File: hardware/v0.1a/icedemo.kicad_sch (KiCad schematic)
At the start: 9 parts

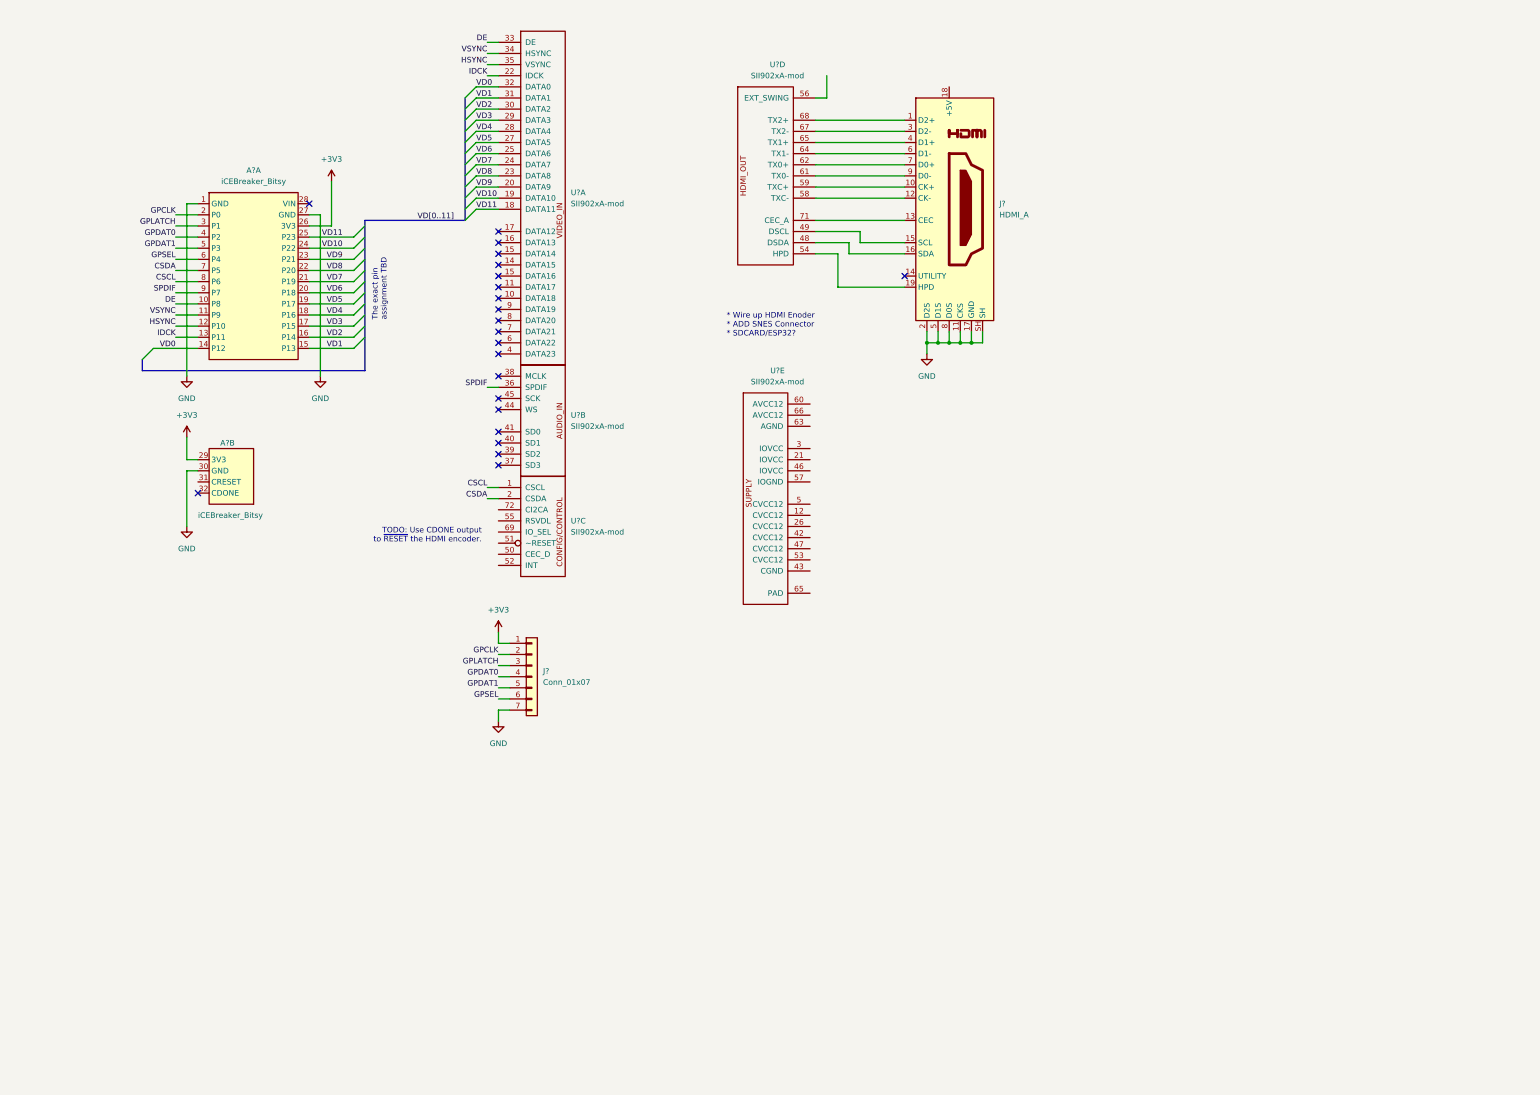
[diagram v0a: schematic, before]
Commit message: First draft of the schematic.
Connected all the remaining pins of the encoder chip.
Replaced the SNES connector generic symbol with a dedicated one.
Added ESD protection to the HDMI connector. (might delete later ;) )
Added level shifters for the SNES interface.
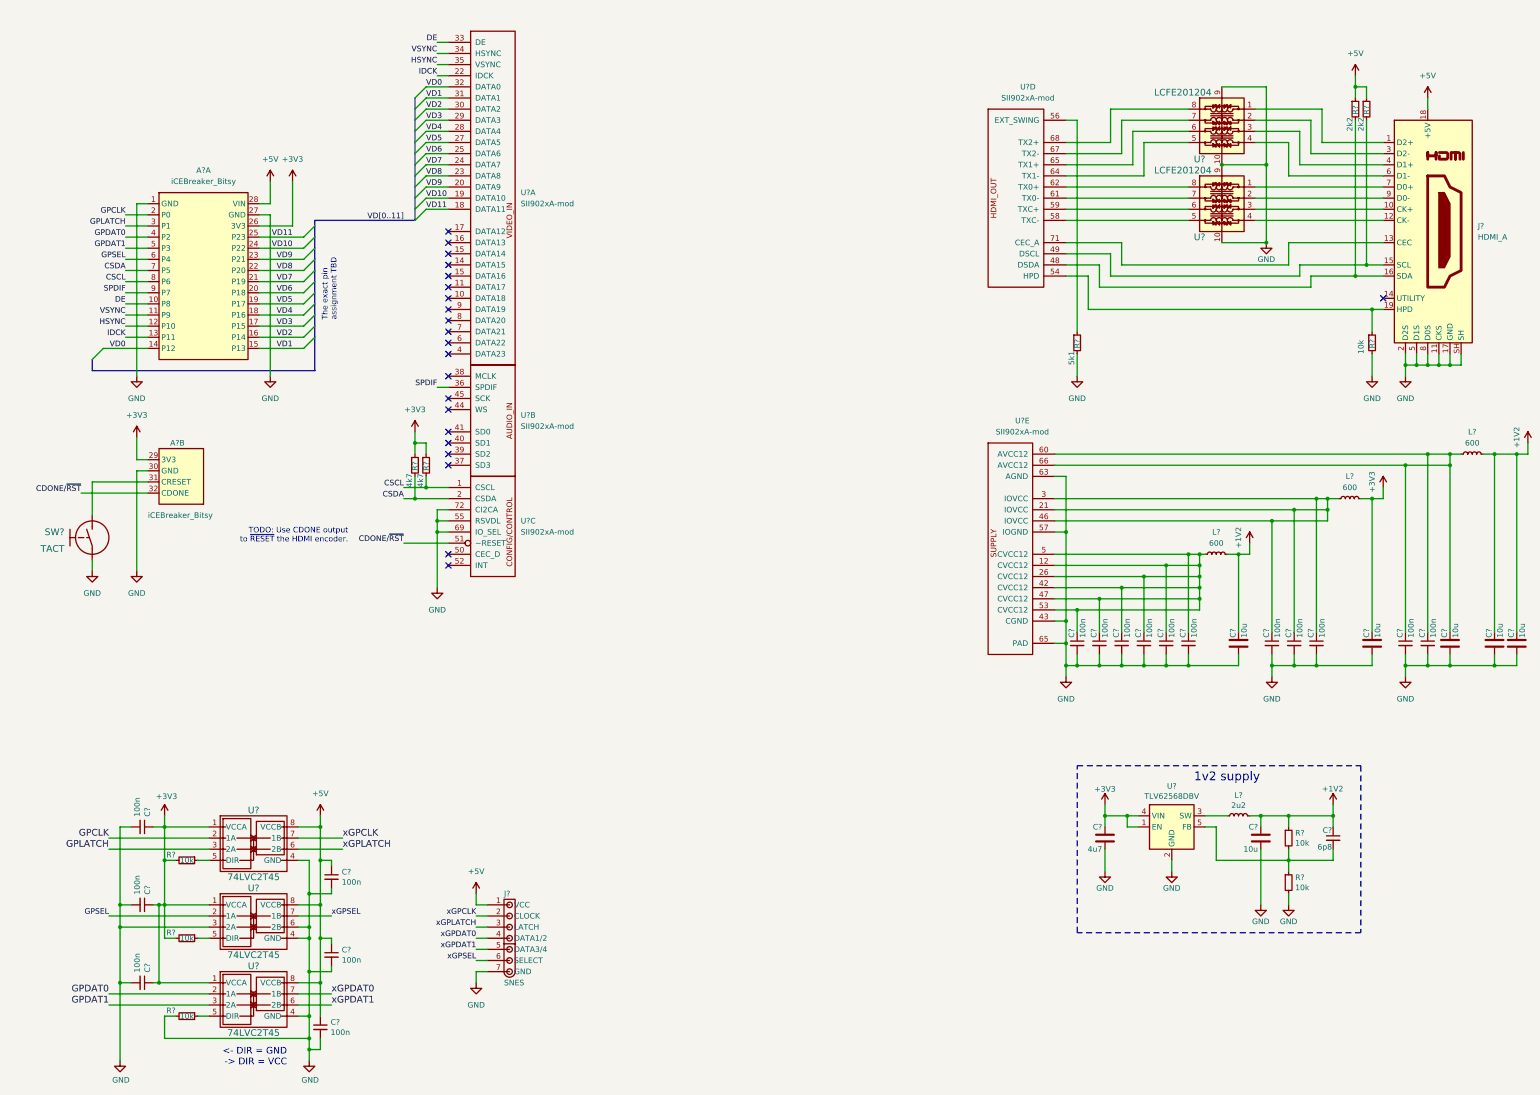
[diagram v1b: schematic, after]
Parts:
- added C?: 6p8, pkl_dipol:C_0402, symbol pkl_device:pkl_C_Small
- added C? (x6): 10u, pkl_dipol:C_0603, symbol pkl_device:pkl_C
- added C? (x17): 100n, pkl_dipol:C_0402, symbol pkl_device:pkl_C_Small
- added C?: 4u7, pkl_dipol:C_0603, symbol pkl_device:pkl_C
- added L?: 2u2, pkl_dipol:L_0805, symbol pkl_device:pkl_L_Small
- added L? (x3): 600, pkl_dipol:L_0402, symbol pkl_device:pkl_L_Small
- added R? (x6): 10k, pkl_dipol:R_0402, symbol pkl_device:pkl_R_Small
- added R? (x2): 2k2, pkl_dipol:R_0402, symbol pkl_device:pkl_R_Small
- added R? (x2): 4k7, pkl_dipol:R_0402, symbol pkl_device:pkl_R_Small
- added R?: 5k1, pkl_dipol:R_0402, symbol pkl_device:pkl_R_Small
- added SW?: TACT, pkl_buttons_switches:SW_SPST_3x4x2.5, symbol pkl_misc:TACT
- added U? (x3): 74LVC2T45, pkl_housings_sot:SOT-833-1, symbol pkl_misc:74LVC2T45
- added U? (x2): LCFE201204, pkl_esd:LCFE201204, symbol pkl_misc:LCFE201204
- added U?: TLV62568DBV, pkl_housings_sot:SOT-23-5, symbol Regulator_Switching:TLV62568DBV
- J?: value Conn_01x07 -> SNES; footprint (none) -> pkl_connectors:SNES; symbol Connector_Generic:Conn_01x07 -> pkl_conn:SNES
- J?: footprint (none) -> pkl_connectors:HDMI-10029449-111RLF
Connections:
- net +3V3: now also C?.1, C?.1, C?.1, C?.1, C?.1, L?.1, R?.1, R?.1, R?.2, R?.2, U?.1 (EN), U?.1 (VCCA), U?.1 (VCCA), U?.1 (VCCA), U?.4 (VIN); no longer J?.1 (Pin_1)
- net CSCL: now also R?.2
- net CSDA: now also R?.2
- net GND: now also U?.43 (CGND), U?.55 (RSVDL), U?.57 (IOGND), U?.63 (AGND), U?.65 (PAD), U?.69 (IO_SEL), U?.72 (CI2CA), C?.2, C?.2, C?.2, C?.2, C?.2, C?.2, C?.2, C?.2, C?.2, C?.2, C?.2, C?.2, C?.2, C?.2, C?.2, C?.2, C?.2, C?.2, C?.2, C?.2, C?.2, C?.2, C?.2, C?.2, R?.2, R?.2, R?.2, R?.2, SW?.1, U?.10, U?.10, U?.2 (GND), U?.3 (2A), U?.4 (GND), U?.4 (GND), U?.4 (GND), U?.6 (2B), U?.9, U?.9
- net GPCLK: now also U?.2 (1A); no longer J?.2 (Pin_2)
- net GPDAT0: now also U?.2 (1A); no longer J?.4 (Pin_4)
- net GPDAT1: now also U?.3 (2A); no longer J?.5 (Pin_5)
- net GPLATCH: now also U?.3 (2A); no longer J?.3 (Pin_3)
- net GPSEL: now also U?.2 (1A); no longer J?.6 (Pin_6)
- net +5V: now reaches A?.28 (VIN)
- net +5V: now also J?.1 (VCC), J?.18 (+5V), C?.1, C?.1, C?.1, R?.1, R?.1, U?.8 (VCCB), U?.8 (VCCB), U?.8 (VCCB)
- net at U?.12 (CVCC12): now also U?.26 (CVCC12), U?.42 (CVCC12), U?.47 (CVCC12), U?.5 (CVCC12), U?.53 (CVCC12), C?.1, C?.1, C?.1, C?.1, C?.1, C?.1, L?.2
- net at U?.21 (IOVCC): now also U?.3 (IOVCC), U?.46 (IOVCC), C?.1, C?.1, C?.1, L?.2
- net at U?.60 (AVCC12): now also U?.66 (AVCC12), C?.1, C?.1, C?.1, L?.2
- net at A?.31 (CRESET): now also SW?.2
- net CDONE/~{RST}: now reaches A?.32 (CDONE)
- net CDONE/~{RST}: now also U?.51 (~RESET)
- net at J?.16 (SDA), U?.48 (DSDA): now also R?.2
- net at J?.15 (SCL), U?.49 (DSCL): now also R?.2
- net at J?.19 (HPD), U?.54 (HPD): now also R?.1
- net at U?.56 (EXT_SWING): now also R?.1
- net at J?.12 (CK-): now also U?.4; no longer U?.58 (TXC-)
- net at J?.10 (CK+): now also U?.3; no longer U?.59 (TXC+)
- net at J?.9 (D0-): now also U?.2; no longer U?.61 (TX0-)
- net at J?.7 (D0+): now also U?.1; no longer U?.62 (TX0+)
- net at J?.6 (D1-): now also U?.4; no longer U?.64 (TX1-)
- net at J?.4 (D1+): now also U?.3; no longer U?.65 (TX1+)
- net at J?.3 (D2-): now also U?.2; no longer U?.67 (TX2-)
- net at J?.1 (D2+): now also U?.1; no longer U?.68 (TX2+)
- new net: C?.2, R?.1, R?.2, U?.5 (FB)
- new net: R?.1, U?.5 (DIR) (x3)
- new net: U?.5, U?.58 (TXC-)
- new net: U?.59 (TXC+), U?.6
- new net: U?.61 (TX0-), U?.7
- new net: U?.62 (TX0+), U?.8
- new net: L?.2, U?.3 (SW)
- new net: U?.5, U?.64 (TX1-)
- new net: U?.6, U?.65 (TX1+)
- new net: U?.67 (TX2-), U?.7
- new net: U?.68 (TX2+), U?.8
- new net +1V2: C?.1, C?.1, C?.1, C?.1, C?.1, L?.1, L?.1, L?.1, R?.1
- new net xGPCLK: J?.2 (CLOCK), U?.7 (1B)
- new net xGPDAT0: J?.4 (DATA1/2), U?.7 (1B)
- new net xGPDAT1: J?.5 (DATA3/4), U?.6 (2B)
- new net xGPLATCH: J?.3 (LATCH), U?.6 (2B)
- new net xGPSEL: J?.6 (SELECT), U?.7 (1B)
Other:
- note added: "1v2 supply"
- note added: "<- DIR = GND -> DIR = VCC"
- note removed: "* Wire up HDMI Enoder * ADD SNES Connector * SDCARD/ESP32?"
- moved on the sheet: A?A, A?B, J?, U?A, U?B, U?C, U?D, U?E

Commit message: Removed ESD protection. It is a toy after all...
* I think it is worth saving $4 over the ESD protection in this case.

Also updated the schematic PDF.
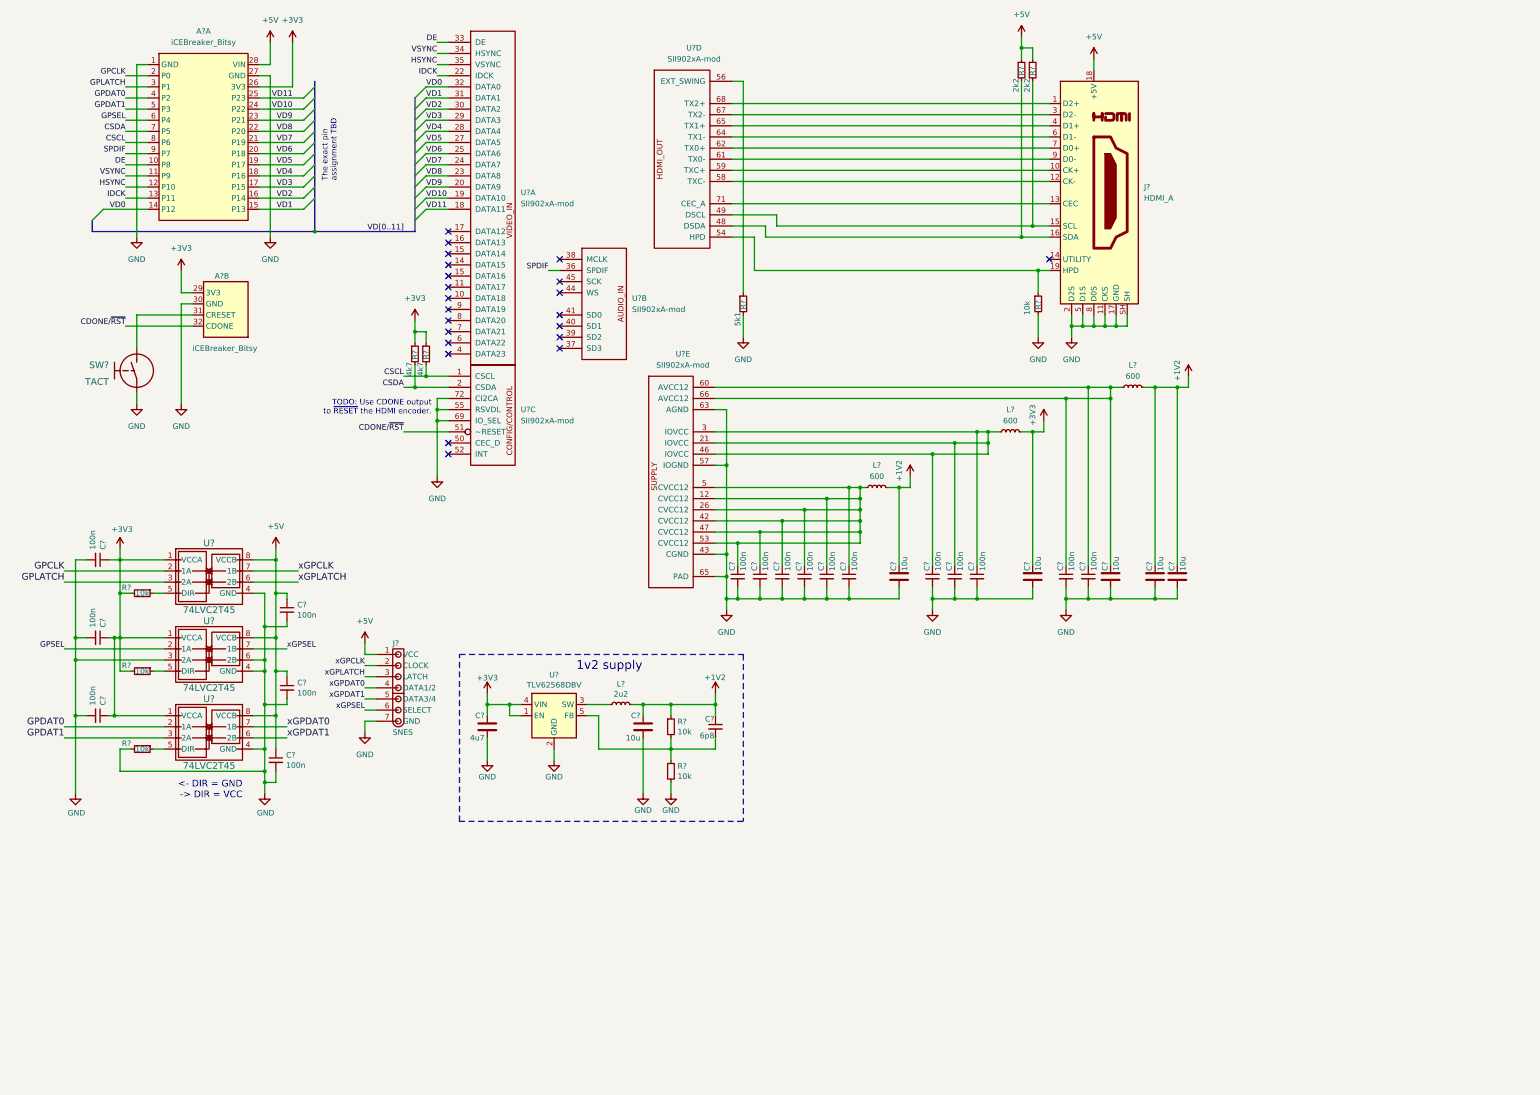
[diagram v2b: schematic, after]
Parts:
- removed U? (x2): LCFE201204, pkl_esd:LCFE201204, symbol pkl_misc:LCFE201204
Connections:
- net at J?.7 (D0+): now also U?.62 (TX0+)
- net at J?.9 (D0-): now also U?.61 (TX0-)
- net at J?.10 (CK+): now also U?.59 (TXC+)
- net at J?.12 (CK-): now also U?.58 (TXC-)
- net at J?.1 (D2+): now also U?.68 (TX2+)
- net at J?.3 (D2-): now also U?.67 (TX2-)
- net at J?.4 (D1+): now also U?.65 (TX1+)
- net at J?.6 (D1-): now also U?.64 (TX1-)
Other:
- moved on the sheet: A?A, A?B, C?, J?, L?, R?, SW?, U?, U?B, U?C, U?D, U?E

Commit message: Improved schematic and started layout.
* Added inline termination resistors.
* Corrected a mistake in the encoder symbol.
  (Pin 15/13 and missing Pin 70)
* Preliminary positioning of the parts on the PCB.
* Started routing the input data pins.
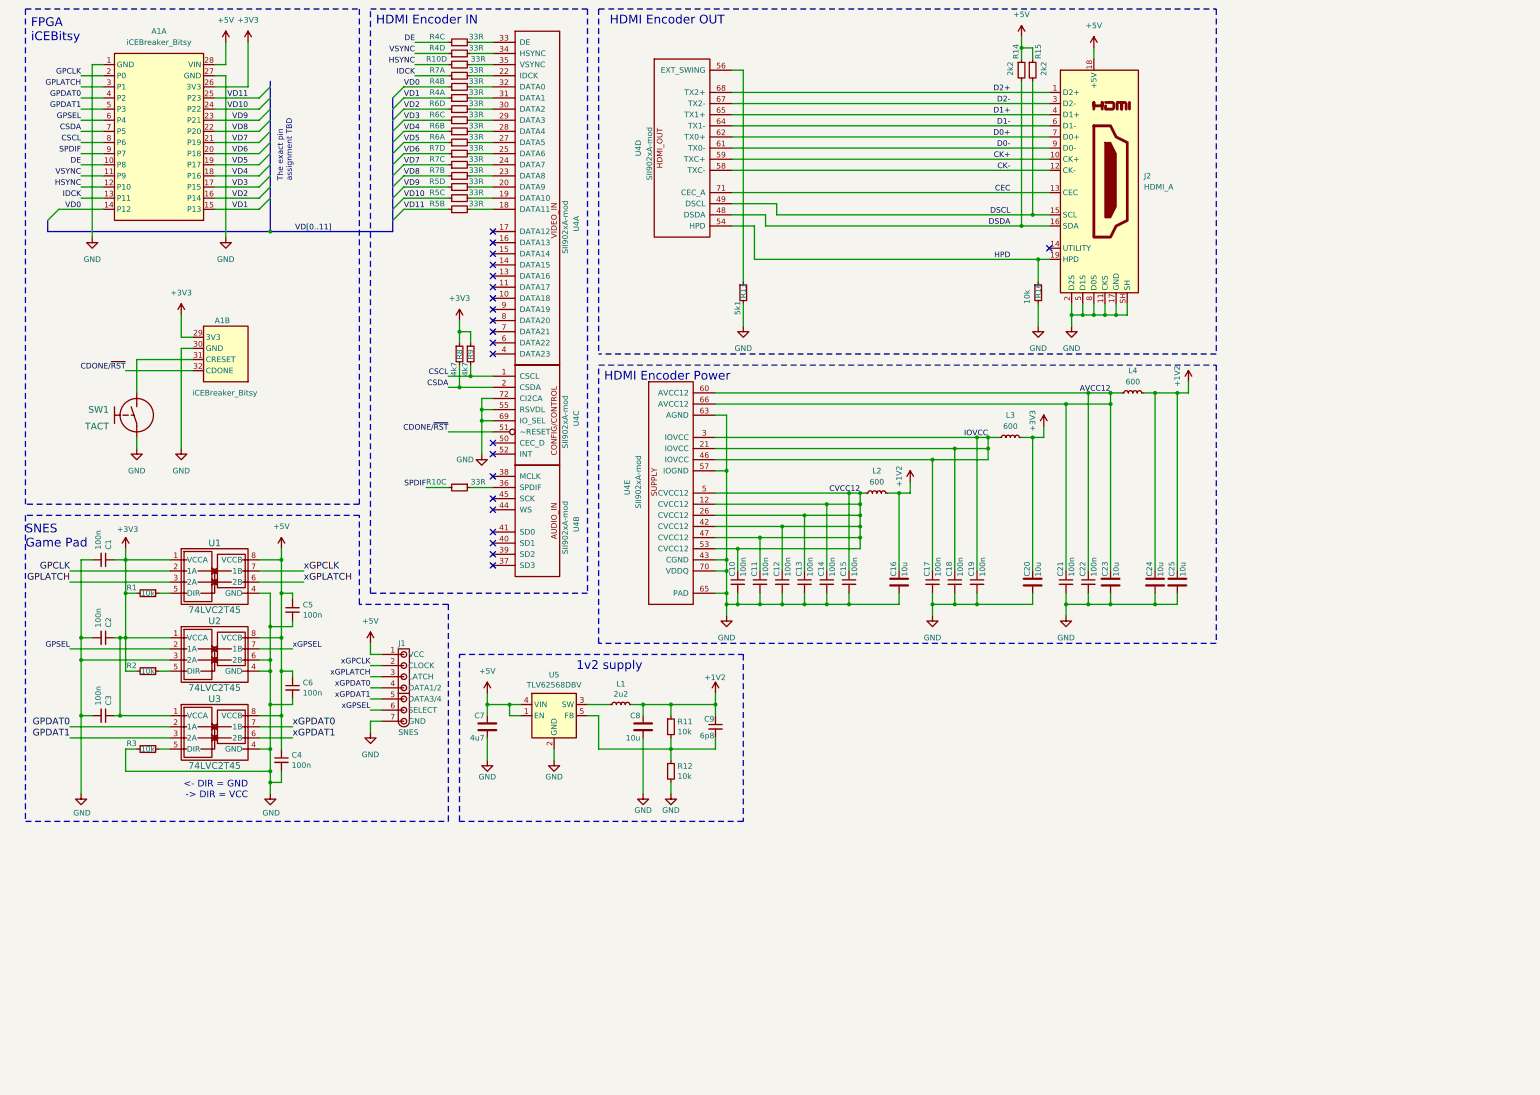
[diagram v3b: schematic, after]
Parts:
- added R10, R4, R5, R6, R7: 33R, pkl_dipol:R_Array_Convex_4x0402, symbol pkl_device:pkl_R4_Small
- U4: renamed from U?; footprint (none) -> Package_DFN_QFN:QFN-72-1EP_10x10mm_P0.5mm_EP6x6mm_ThermalVias
- gave numbers to parts that had none: 48
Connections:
- net +3V3: no longer C7.1, U5.1 (EN), U5.4 (VIN)
- net +5V: now also C7.1, U5.1 (EN), U5.4 (VIN)
- net DE: now also R4.5; no longer U4.33 (DE)
- net GND: now also U4.70 (VDDQ)
- net HSYNC: now also R10.8; no longer U4.35 (VSYNC)
- net IDCK: now also R7.1; no longer U4.22 (IDCK)
- net SPDIF: now also R10.6; no longer U4.36 (SPDIF)
- net VD0: now also R4.3; no longer U4.32 (DATA0)
- net VD1: now also R4.1; no longer U4.31 (DATA1)
- net VD10: now also R5.5; no longer U4.19 (DATA10)
- net VD11: now also R5.3; no longer U4.18 (DATA11)
- net VD2: now also R6.7; no longer U4.30 (DATA2)
- net VD3: now also R6.5; no longer U4.29 (DATA3)
- net VD4: now also R6.3; no longer U4.28 (DATA4)
- net VD5: now also R6.1; no longer U4.27 (DATA5)
- net VD6: now also R7.7; no longer U4.25 (DATA6)
- net VD7: now also R7.5; no longer U4.24 (DATA7)
- net VD8: now also R7.3; no longer U4.23 (DATA8)
- net VD9: now also R5.7; no longer U4.20 (DATA9)
- net VSYNC: now also R4.7; no longer U4.34 (HSYNC)
- net AVCC12: now reaches C21.1, C22.1, C23.1, L4.2, U4.60 (AVCC12), U4.66 (AVCC12)
- net DSCL: now reaches J2.15 (SCL), R15.2, U4.49 (DSCL)
- net CVCC12: now reaches C10.1, C11.1, C12.1, C13.1, C14.1, C15.1, L2.2, U4.12 (CVCC12), U4.26 (CVCC12), U4.42 (CVCC12), U4.47 (CVCC12), U4.5 (CVCC12), U4.53 (CVCC12)
- net DSDA: now reaches J2.16 (SDA), R14.2, U4.48 (DSDA)
- net IOVCC: now reaches C17.1, C18.1, C19.1, L3.2, U4.21 (IOVCC), U4.3 (IOVCC), U4.46 (IOVCC)
- net HPD: now reaches J2.19 (HPD), R16.1, U4.54 (HPD)
- net CK-: now reaches J2.12 (CK-), U4.58 (TXC-)
- net CK+: now reaches J2.10 (CK+), U4.59 (TXC+)
- net D0-: now reaches J2.9 (D0-), U4.61 (TX0-)
- net D0+: now reaches J2.7 (D0+), U4.62 (TX0+)
- net D1-: now reaches J2.6 (D1-), U4.64 (TX1-)
- net D1+: now reaches J2.4 (D1+), U4.65 (TX1+)
- net D2-: now reaches J2.3 (D2-), U4.67 (TX2-)
- net D2+: now reaches J2.1 (D2+), U4.68 (TX2+)
- net CEC: now reaches J2.13 (CEC), U4.71 (CEC_A)
- new net: R10.5, U4.36 (SPDIF)
- new net: R6.2, U4.27 (DATA5)
- new net: R4.4, U4.32 (DATA0)
- new net: R10.7, U4.35 (VSYNC)
- new net: R6.4, U4.28 (DATA4)
- new net: R6.6, U4.29 (DATA3)
- new net: R4.6, U4.33 (DE)
- new net: R7.8, U4.25 (DATA6)
- new net: R5.6, U4.19 (DATA10)
- new net: R7.4, U4.23 (DATA8)
- new net: R7.2, U4.22 (IDCK)
- new net: R6.8, U4.30 (DATA2)
- new net: R5.4, U4.18 (DATA11)
- new net: R4.8, U4.34 (HSYNC)
- new net: R7.6, U4.24 (DATA7)
- new net: R4.2, U4.31 (DATA1)
- new net: R5.8, U4.20 (DATA9)
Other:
- note added: "FPGA iCEBitsy"
- note added: "HDMI Encoder IN"
- note added: "HDMI Encoder OUT"
- note added: "HDMI Encoder Power"
- note added: "SNES Game Pad"
- note removed: "TODO: Use CDONE output to ~{RESET} the HDMI encoder."
- moved on the sheet: A1A, A1B, C1, C10, C11, C12, C13, C14, C15, C16, C17, C18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
